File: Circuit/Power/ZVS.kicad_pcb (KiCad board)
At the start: 2 copper layers, 81.3 x 73.7 mm, 17 parts, among them J1 12V DC in, J2 12V AC out, Q1 IRFP250, Q2 IRFP250, T1 10:10

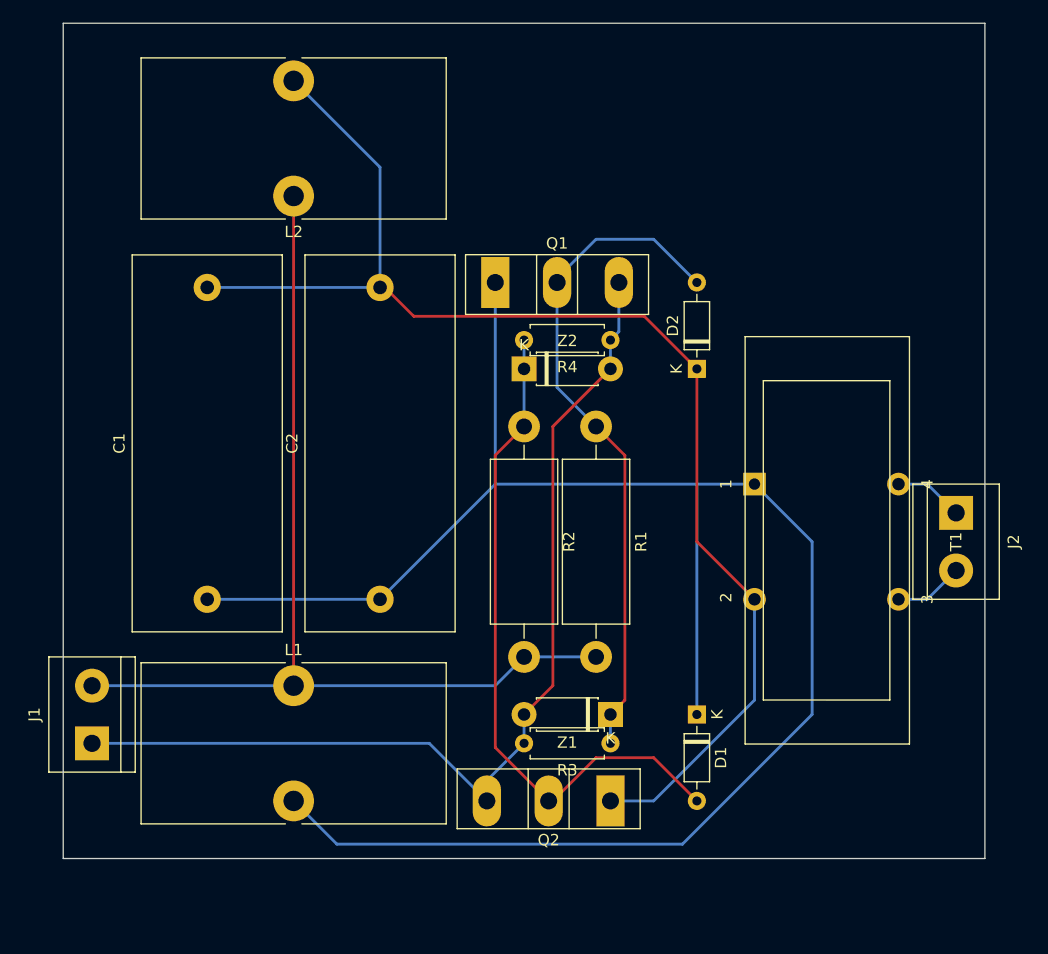
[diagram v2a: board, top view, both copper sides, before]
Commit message: [Circuit][Doc] Remove the transformer from ZVS module
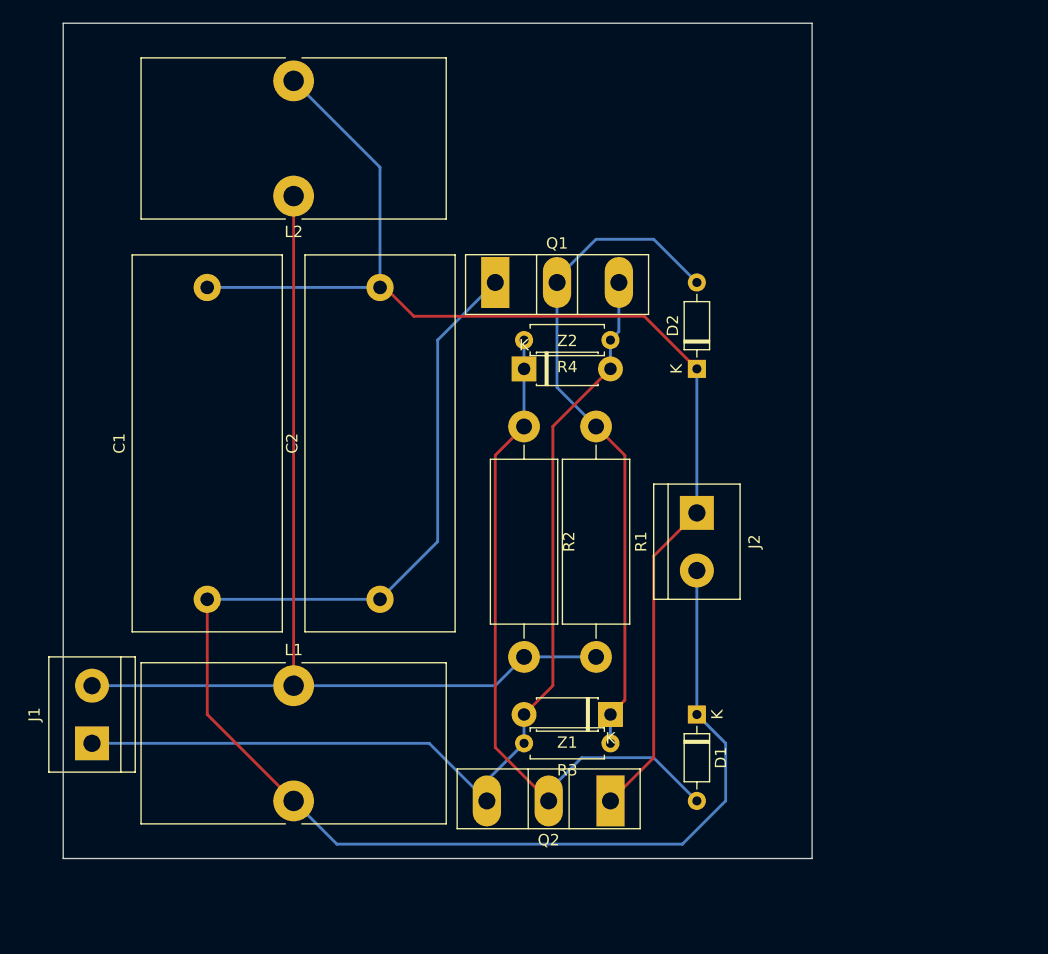
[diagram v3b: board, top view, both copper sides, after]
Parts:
- removed T1: 10:10, Power:Transformer_Toroid_4Pin
- J2: value 12V AC out -> Output
- moved J2 22.9 mm to (149.9, 50.8)
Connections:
- C1 pad 1: Net-(C1-Pad1) -> /Output+
- C1 pad 2: Net-(C1-Pad2) -> /Output-
- C2 pad 1: Net-(C1-Pad1) -> /Output+
- C2 pad 2: Net-(C1-Pad2) -> /Output-
- D1 pad 1: Net-(C1-Pad1) -> /Output+
- D2 pad 1: Net-(C1-Pad2) -> /Output-
- J2 pad 1: /ACOutput+ -> /Output-
- J2 pad 2: /ACOutput- -> /Output+
- L1 pad 2: Net-(C1-Pad1) -> /Output+
- L2 pad 2: Net-(C1-Pad2) -> /Output-
- Q1 pad 1: Net-(C1-Pad1) -> /Output+
- Q2 pad 1: Net-(C1-Pad2) -> /Output-
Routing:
- net Net-(C1-Pad1): track 165.0 -> 0.00 mm
- net /Output+: track 0.00 -> 131.0 mm
- net Net-(C1-Pad2): track 115.2 -> 0.00 mm
- net /Output-: track 0.00 -> 108.8 mm
- net /ACOutput-: track 6.13 -> 0.00 mm
- net /ACOutput+: track 6.13 -> 0.00 mm
- net Net-(D1-Pad2): track 59.9 -> 60.8 mm
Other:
- board size 81.3 x 73.7 mm -> 66 x 73.7 mm

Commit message: [Circuit] Adjust the track width in ZVS module
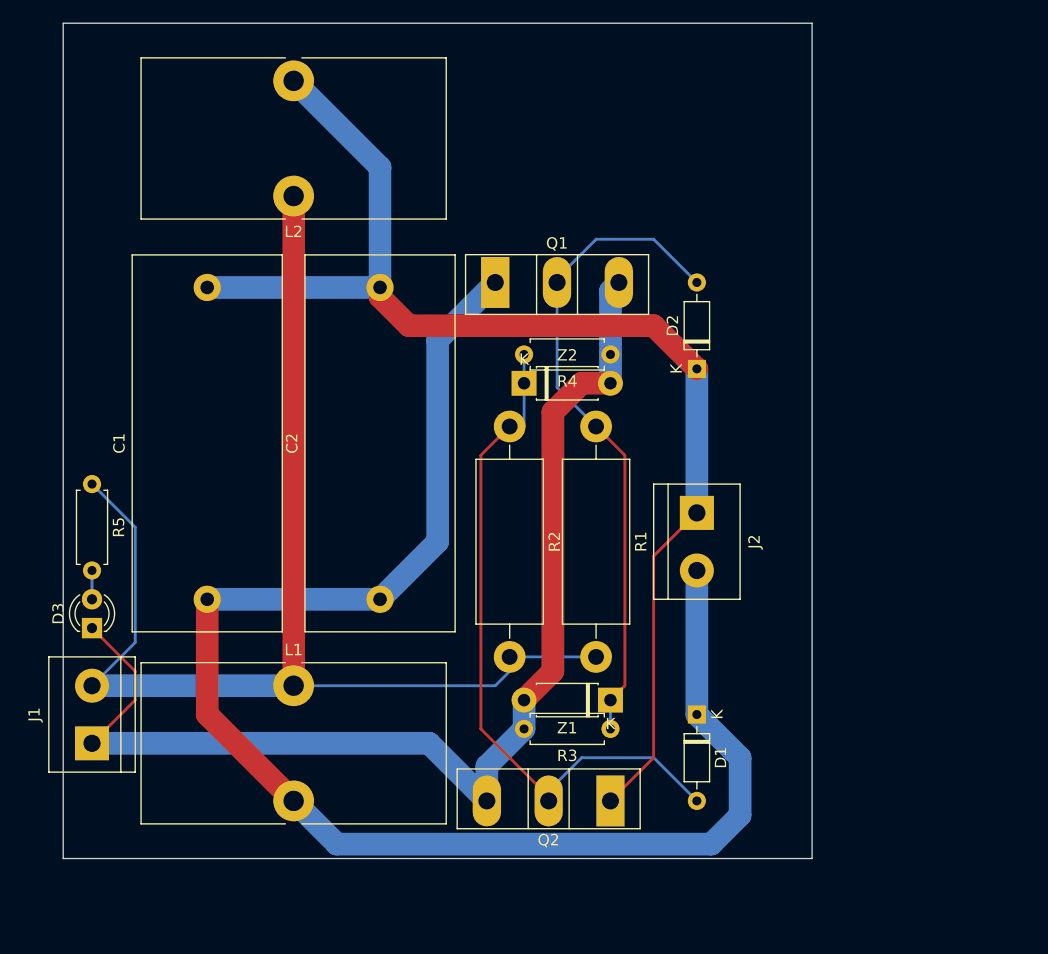
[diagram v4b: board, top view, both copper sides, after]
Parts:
- added D3: LED, LED_THT:LED_D3.0mm_FlatTop, F.Cu at (96.5, 61.0)
- added R5: 2.2K, Resistor_THT:R_Axial_DIN0207_L6.3mm_D2.5mm_P7.62mm_Horizontal, F.Cu at (96.5, 48.3)
- moved R2 1.27 mm to (133.3, 43.2)
- moved R3 1.27 mm to (142.2, 69.8)
- moved R4 1.27 mm to (142.2, 36.8)
- moved Z1 1.27 mm to (142.2, 67.3)
- moved Z2 1.27 mm to (134.6, 39.4)
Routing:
- net /DCInput+: track 88.7 -> 109.6 mm
- net /DCInput-: track 87.5 -> 102.3 mm
- net Net-(D3-Pad2): track 0.00 -> 2.54 mm
- net /Output+: track 131.0 -> 133.5 mm
- net Net-(D2-Pad2): track 59.3 -> 58.1 mm
- net /Output-: track 108.8 -> 109.7 mm
- net Net-(D1-Pad2): track 60.8 -> 60.0 mm

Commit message: [Circuit] Upgrade to KiCad 6 format
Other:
- net class Default removed

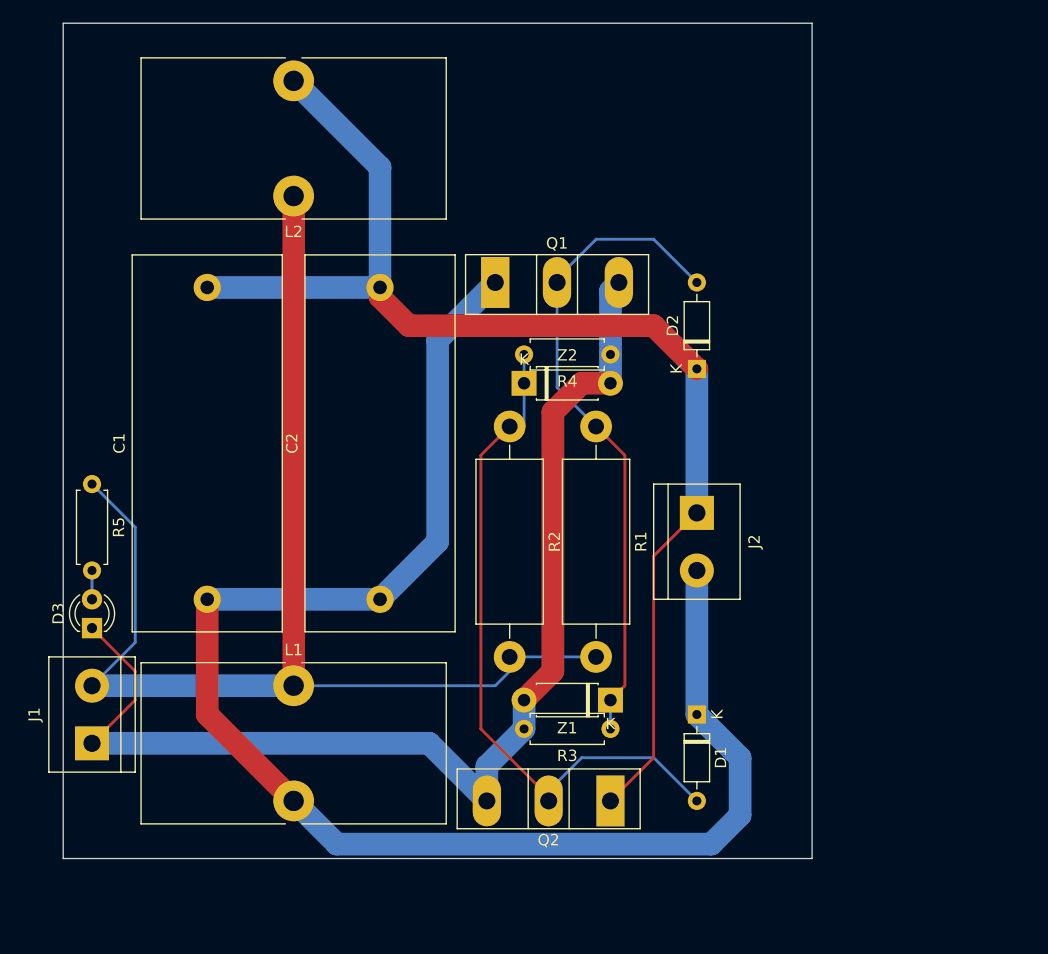
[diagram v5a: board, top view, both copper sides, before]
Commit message: [Circuit] High frequency ZVS module with gate driver
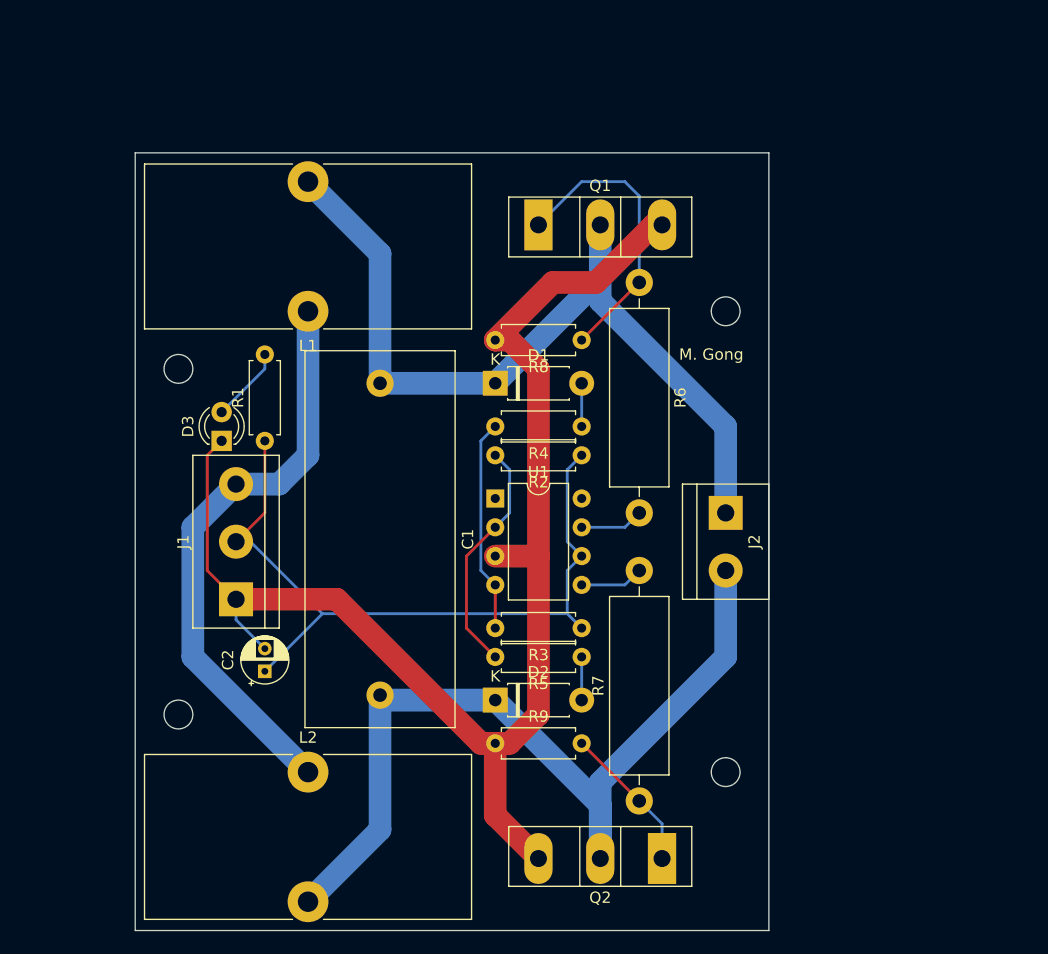
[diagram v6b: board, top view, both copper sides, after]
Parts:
- removed the R1 at (141.0, 43.2)
- removed Z1, Z2: 1N4742, Diode_THT:D_DO-41_SOD81_P7.62mm_Horizontal
- added R3: 3.3K, Resistor_THT:R_Axial_DIN0207_L6.3mm_D2.5mm_P7.62mm_Horizontal, F.Cu at (139.7, 61.0)
- added R4: 100, Resistor_THT:R_Axial_DIN0207_L6.3mm_D2.5mm_P7.62mm_Horizontal, F.Cu at (139.7, 43.2)
- added R5: 100, Resistor_THT:R_Axial_DIN0207_L6.3mm_D2.5mm_P7.62mm_Horizontal, F.Cu at (139.7, 63.5)
- added R6: 10R 5W, Resistor_THT:R_Axial_DIN0516_L15.5mm_D5.0mm_P20.32mm_Horizontal, F.Cu at (144.8, 30.5)
- added R7: 10R 5W, Resistor_THT:R_Axial_DIN0516_L15.5mm_D5.0mm_P20.32mm_Horizontal, F.Cu at (144.8, 76.2)
- added U1: UCC27524P, Package_DIP:DIP-8_W7.62mm, F.Cu at (132.1, 49.5)
- C2: value MKP 0.33uF -> 10uF; footprint Capacitor_THT:C_Rect_L33.0mm_W13.0mm_P27.50mm_MKS4 -> Capacitor_THT:CP_Radial_D4.0mm_P2.00mm
- D1, D2: value FR107 -> UF4007; footprint Diode_THT:D_DO-35_SOD27_P7.62mm_Horizontal -> Diode_THT:D_DO-41_SOD81_P7.62mm_Horizontal
- J1: footprint TerminalBlock:TerminalBlock_bornier-2_P5.08mm -> TerminalBlock:TerminalBlock_bornier-3_P5.08mm
- L1, L2: footprint Inductor_THT:L_Toroid_Vertical_L26.7mm_W14.0mm_P10.16mm_Pulse_D -> Inductor_THT:L_Toroid_Vertical_L28.6mm_W14.3mm_P11.43mm_Bourns_5700
- R2: value 470 2W -> 3.3K; footprint Resistor_THT:R_Axial_DIN0614_L14.3mm_D5.7mm_P20.32mm_Horizontal -> Resistor_THT:R_Axial_DIN0207_L6.3mm_D2.5mm_P7.62mm_Horizontal
- moved L2 50.8 mm to (115.6, 73.7), turned to 0 degrees
- moved R9 35.8 mm to (132.1, 71.1), turned to 0 degrees
- moved R8 34.4 mm to (139.7, 35.6)
- moved D1 34.2 mm to (132.1, 39.4), turned to 0 degrees
- moved D2 34.2 mm to (132.1, 67.3), turned to 0 degrees
- moved L1 33.0 mm to (115.6, 33.0), turned to 180 degrees
- moved C1 24.4 mm to (121.9, 39.4), turned to -90 degrees
- moved D3 20.1 mm to (108.0, 44.5)
- moved J1 18.0 mm to (109.2, 58.4)
- moved R1 15.7 mm to (111.8, 44.5), turned to 90 degrees
- moved C2 12.0 mm to (111.8, 64.8)
- moved R2 6.84 mm to (139.7, 45.7), turned to 180 degrees
- moved Q2 6.82 mm to (146.8, 81.3)
- moved Q1 6.35 mm to (135.9, 25.4)
- moved J2 2.54 mm to (152.4, 50.8)
- renumbered R5 to R1, R3 to R8, R4 to R9
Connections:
- C2 pad 1: /Output+ -> /DCInput+
- C2 pad 2: /Output- -> GND
- D3 pad 1: /DCInput- -> GND
- J1 pad 1: /DCInput- -> GND
- J2 pad 1: /Output- -> /Output+
- J2 pad 2: /Output+ -> /Output-
- L1 pad 1: /DCInput+ -> Net-(J1-Pad3)
- L2 pad 1: /DCInput+ -> Net-(J1-Pad3)
- Q1 pad 1: /Output+ -> Net-(Q1-Pad1)
- Q1 pad 2: Net-(D2-Pad2) -> /Output+
- Q1 pad 3: /DCInput- -> GND
- Q2 pad 1: /Output- -> Net-(Q2-Pad1)
- Q2 pad 2: Net-(D1-Pad2) -> /Output-
- Q2 pad 3: /DCInput- -> GND
- R2 pad 1: Net-(D1-Pad2) -> /DCInput+
- R2 pad 2: /DCInput+ -> Net-(R2-Pad2)
- R8 pad 1: Net-(D2-Pad2) -> Net-(Q1-Pad1)
- R8 pad 2: /DCInput- -> GND
- R9 pad 1: /DCInput- -> GND
- R9 pad 2: Net-(D1-Pad2) -> Net-(Q2-Pad1)
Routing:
- net GND: track 0.00 -> 123.7 mm
- net /DCInput-: track 102.3 -> 0.00 mm
- net /Output+: track 133.5 -> 73.6 mm
- net Net-(D1-Pad2): track 60.0 -> 3.81 mm
- net Net-(D2-Pad2): track 58.1 -> 3.81 mm
- net Net-(J1-Pad3): track 0.00 -> 51.3 mm
- net /DCInput+: track 109.6 -> 66.3 mm
- net /Output-: track 109.7 -> 79.0 mm
- net Net-(Q1-Pad1): track 0.00 -> 25.8 mm
- net Net-(R2-Pad2): track 0.00 -> 20.9 mm
- net Net-(R3-Pad2): track 0.00 -> 18.8 mm
- net Net-(Q2-Pad1): track 0.00 -> 13.1 mm
- net Net-(R6-Pad2): track 0.00 -> 5.61 mm
- net Net-(R7-Pad2): track 0.00 -> 5.61 mm
- net Net-(D3-Pad2): track 2.54 -> 6.66 mm
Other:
- board size 66 x 73.7 mm -> 55.9 x 68.6 mm
- board text added: "M. Gong"
